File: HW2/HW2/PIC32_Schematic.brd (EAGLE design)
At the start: 50 x 50 mm, 22 parts

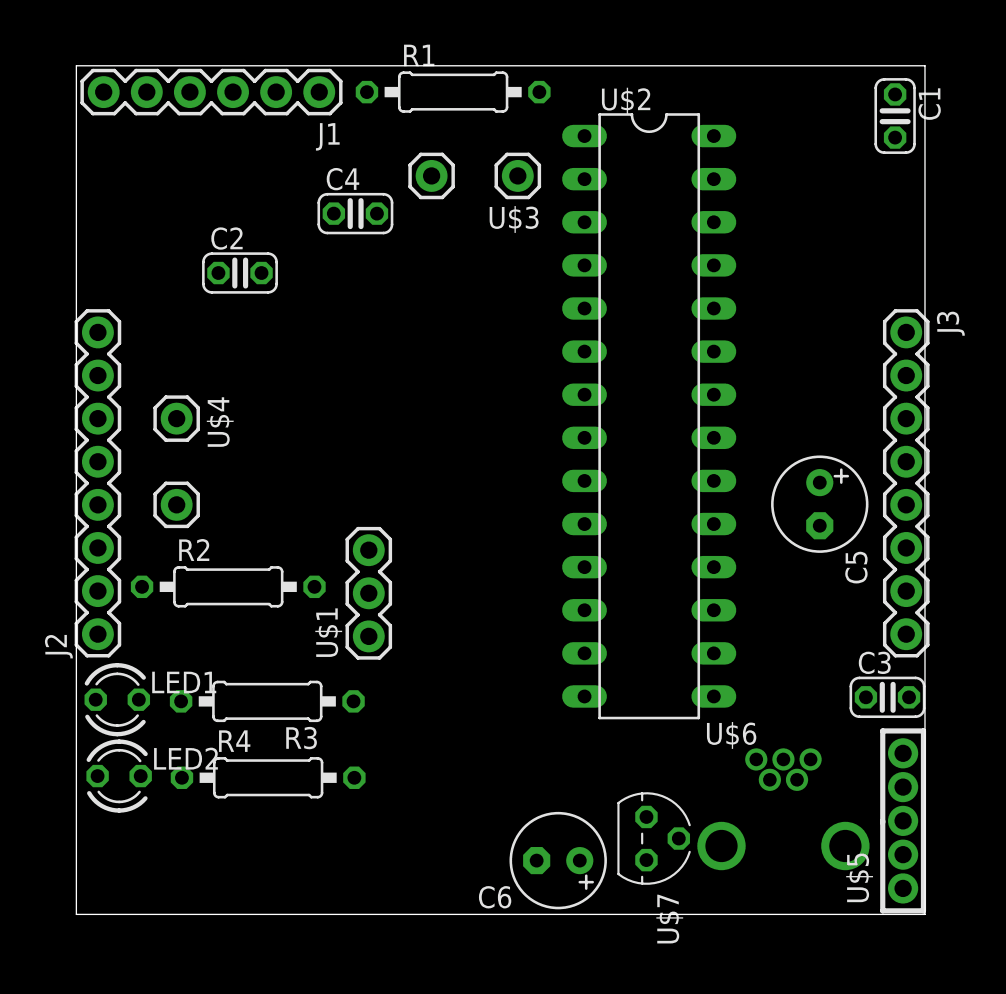
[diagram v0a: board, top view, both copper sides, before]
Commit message: All components placed relative to each other
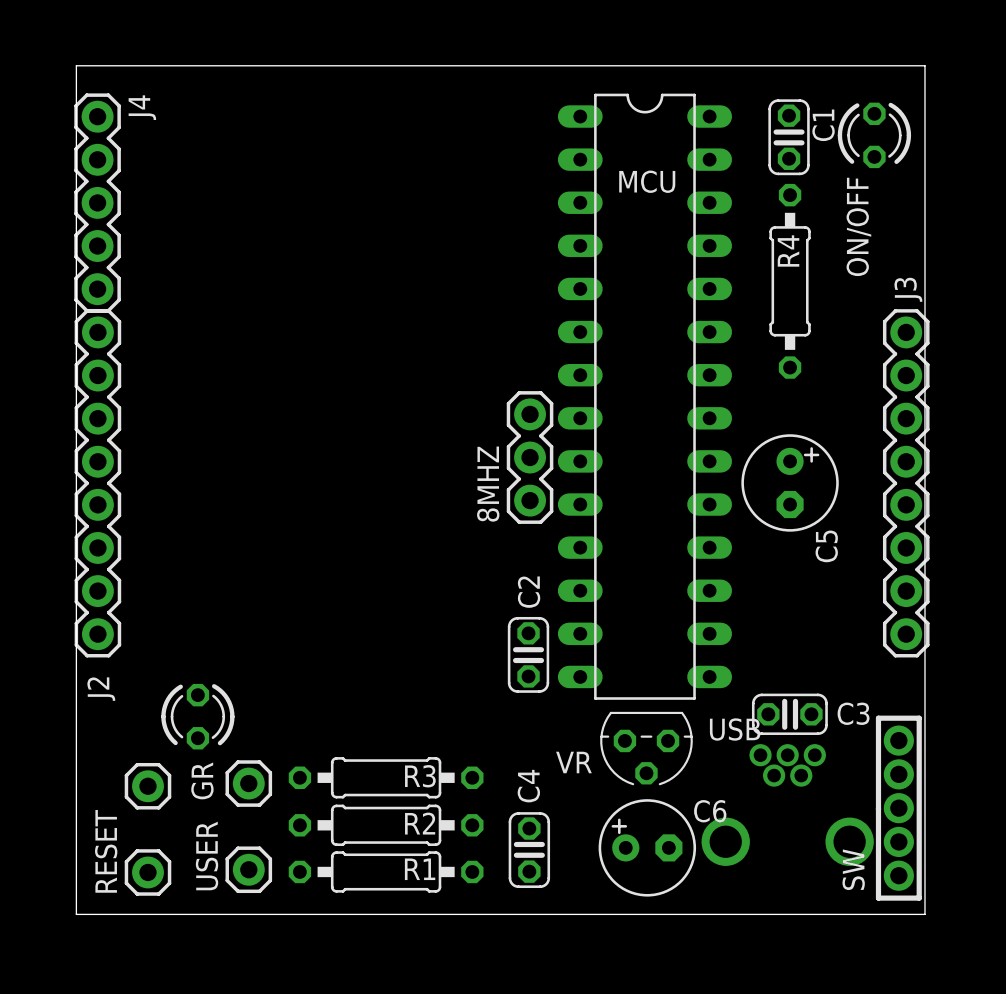
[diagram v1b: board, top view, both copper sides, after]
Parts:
- removed J1: (no value), ME433:1X06
- removed LED1: GREEN, ME433:LED3MM
- removed LED2: RED, ME433:LED3MM
- removed U$1: 8MHZ_XTAL, ME433:8MHZ_XTAL
- removed U$2: PIC32MX250F128B, ME433:DIL28-3
- removed U$3, U$4: PUSH-BUTTON, ME433:PUSH-BUTTON
- removed U$5: SLIDE_SWITCH, ME433:SLIDE_SWITCH
- removed U$6: USB-MB-H-5PIN, ME433:USB-MB-H
- removed U$7: MCP1702, ME433:TO92
- added 8MHZ: XTAL, ME433:8MHZ_XTAL
- added GR: RA4, ME433:LED3MM
- added J4: (no value), ME433:1X05
- added MCU: PIC32MX250F128B, ME433:DIL28-3
- added ON/OFF: (no value), ME433:LED3MM
- added RESET, USER: (no value), ME433:PUSH-BUTTON
- added SW: (no value), ME433:SLIDE_SWITCH
- added USB: USB-MB-H-5PIN, ME433:USB-MB-H
- added VR: MCP1702, ME433:TO92
- moved R1 46.1 mm to (18.2, 2.50)
- moved R4 42.4 mm to (42.0, 37.3), turned to 270 degrees
- moved C4 38.9 mm to (26.7, 3.79), turned to 90 degrees
- moved C2 28.2 mm to (26.6, 15.3), turned to 270 degrees
- moved R2 16.8 mm to (18.2, 5.25), turned to 180 degrees
- moved R3 8.32 mm to (18.2, 8.05)
- moved C1 6.37 mm to (42.0, 45.8)
- moved C3 5.84 mm to (42.0, 11.8)
- moved C6 5.30 mm to (33.6, 3.92), turned to 0 degrees
- moved C5 2.15 mm to (42.0, 25.4)
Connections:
- net +3V3: now also J4.2, MCU.13, MCU.23, MCU.28, ON/OFF.A, VR.3; no longer J1.2, LED2.A, U$2.13, U$2.23, U$2.28, U$7.3
- net +5V: now also MCU.15, SW.4, VR.2; no longer U$2.15, U$5.4, U$7.2
- net A0: now also MCU.2; no longer U$2.2
- net A1: now also MCU.3; no longer U$2.3
- net A2: now also 8MHZ.3, MCU.9; no longer U$1.3, U$2.9
- net A3: now also 8MHZ.1, MCU.10; no longer U$1.1, U$2.10
- net A4: now also GR.A, MCU.12; no longer LED1.A, U$2.12
- net B0: now also J4.4, MCU.4; no longer J1.4, U$2.4
- net B1: now also J4.5, MCU.5; no longer J1.5, U$2.5
- net B13: now also MCU.24; no longer U$2.24
- net B14: now also MCU.25; no longer U$2.25
- net B15: now also MCU.26; no longer U$2.26
- net B2: now also MCU.6; no longer U$2.6
- net B3: now also MCU.7; no longer U$2.7
- net B4: now also MCU.11, USER.3; no longer U$2.11, U$4.3
- net B7: now also MCU.16; no longer U$2.16
- net B8: now also MCU.17; no longer U$2.17
- net B9: now also MCU.18; no longer U$2.18
- net D+: now also MCU.21, USB.D+; no longer U$2.21, U$6.D+
- net D-: now also MCU.22, USB.D-; no longer U$2.22, U$6.D-
- net GND: now also 8MHZ.2, J4.3, MCU.19, MCU.27, MCU.8, RESET.1, USB.GND, USER.1, VR.1; no longer J1.3, U$1.2, U$2.19, U$2.27, U$2.8, U$3.1, U$4.1, U$6.GND, U$7.1
- net GREENLED: now also GR.K; no longer LED1.K
- net ID: now also MCU.14, USB.ID; no longer U$2.14, U$6.ID
- net MCLR: now also J4.1, MCU.1, RESET.3; no longer J1.1, U$2.1, U$3.3
- net N$3: now also ON/OFF.K; no longer LED2.K
- net N$9: now also MCU.20; no longer U$2.20
- net VBUS: now also SW.3, USB.VBUS; no longer U$5.3, U$6.VBUS

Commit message: Ground and +3.3V planes added (bottom and top)
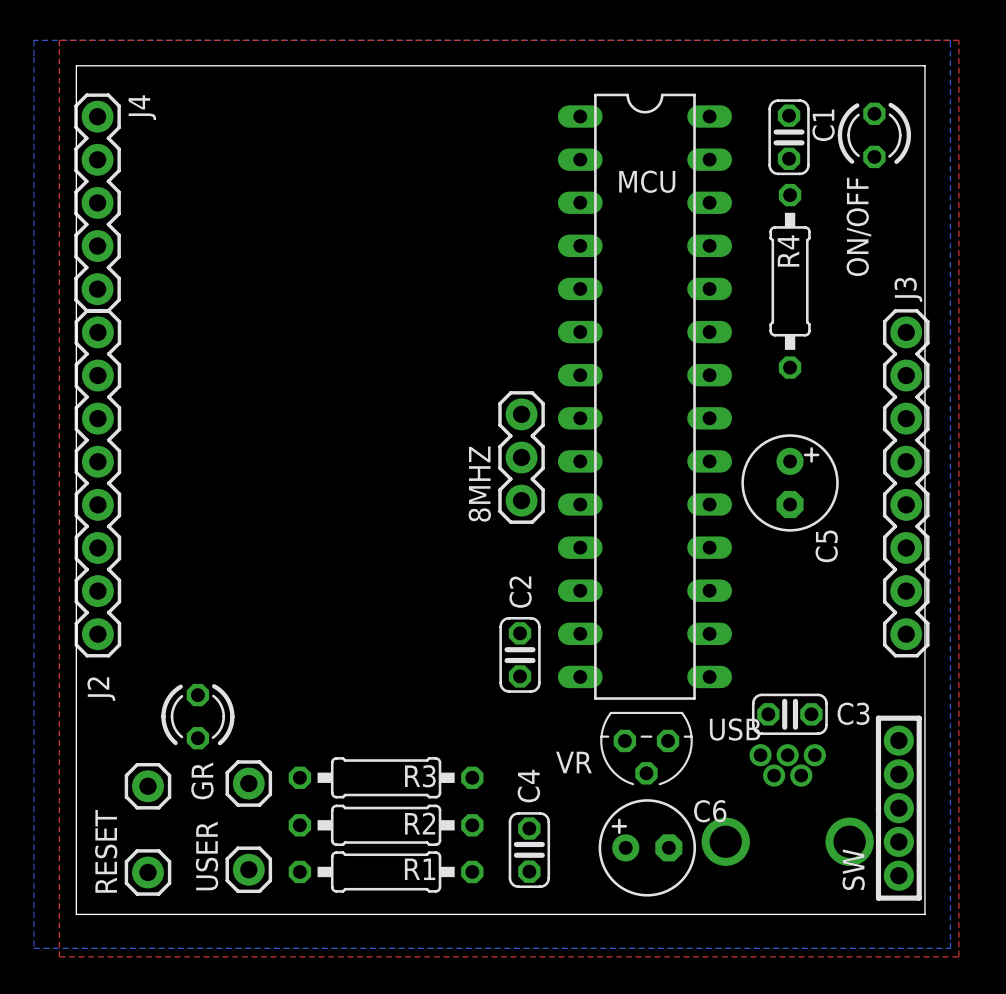
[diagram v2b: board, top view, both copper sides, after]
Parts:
- moved 8MHZ 0.50 mm to (26.2, 26.9)
- moved C2 0.50 mm to (26.1, 15.3)
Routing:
- added copper zone on layer 1, net +3V3
- added copper zone on layer 16, net GND
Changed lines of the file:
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@@
 <layers>
 <layer number="1" name="Top" color="4" fill="1" visible="yes" active="yes"/>
-<layer number="16" name="Bottom" color="1" fill="1" visible="yes" active="yes"/>
+<layer number="16" name="GND" color="1" fill="1" visible="yes" active="yes"/>
 <layer number="17" name="Pads" color="2" fill="1" visible="yes" active="yes"/>
 <layer number="18" name="Vias" color="2" fill="1" visible="yes" active="yes"/>
@@
 <layer number="27" name="tValues" color="7" fill="1" visible="yes" active="yes"/>
 <layer number="28" name="bValues" color="7" fill="1" visible="yes" active="yes"/>
-<layer number="29" name="tStop" color="7" fill="3" visible="no" active="yes"/>
-<layer number="30" name="bStop" color="7" fill="6" visible="no" active="yes"/>
-<layer number="31" name="tCream" color="7" fill="4" visible="no" active="yes"/>
-<layer number="32" name="bCream" color="7" fill="5" visible="no" active="yes"/>
-<layer number="33" name="tFinish" color="6" fill="3" visible="no" active="yes"/>
-<layer number="34" name="bFinish" color="6" fill="6" visible="no" active="yes"/>
-<layer number="35" name="tGlue" color="7" fill="4" visible="no" active="yes"/>
-<layer number="36" name="bGlue" color="7" fill="5" visible="no" active="yes"/>
-<layer number="37" name="tTest" color="7" fill="1" visible="no" active="yes"/>
-<layer number="38" name="bTest" color="7" fill="1" visible="no" active="yes"/>
+<layer number="29" name="tStop" color="7" fill="3" visible="yes" active="yes"/>
+<layer number="30" name="bStop" color="7" fill="6" visible="yes" active="yes"/>
+<layer number="31" name="tCream" color="7" fill="4" visible="yes" active="yes"/>
+<layer number="32" name="bCream" color="7" fill="5" visible="yes" active="yes"/>
+<layer number="33" name="tFinish" color="6" fill="3" visible="yes" active="yes"/>
+<layer number="34" name="bFinish" color="6" fill="6" visible="yes" active="yes"/>
+<layer number="35" name="tGlue" color="7" fill="4" visible="yes" active="yes"/>
+<layer number="36" name="bGlue" color="7" fill="5" visible="yes" active="yes"/>
+<layer number="37" name="tTest" color="7" fill="1" visible="yes" active="yes"/>
+<layer number="38" name="bTest" color="7" fill="1" visible="yes" active="yes"/>
 <layer number="39" name="tKeepout" color="4" fill="11" visible="yes" active="yes"/>
 <layer number="40" name="bKeepout" color="1" fill="11" visible="yes" active="yes"/>
@@
 <layer number="42" name="bRestrict" color="1" fill="10" visible="yes" active="yes"/>
 <layer number="43" name="vRestrict" color="2" fill="10" visible="yes" active="yes"/>
-<layer number="44" name="Drills" color="7" fill="1" visible="no" active="yes"/>
-<layer number="45" name="Holes" color="7" fill="1" visible="no" active="yes"/>
-<layer number="46" name="Milling" color="3" fill="1" visible="no" active="yes"/>
-<layer number="47" name="Measures" color="7" fill="1" visible="no" active="yes"/>
+<layer number="44" name="Drills" color="7" fill="1" visible="yes" active="yes"/>
+<layer number="45" name="Holes" color="7" fill="1" visible="yes" active="yes"/>
+<layer number="46" name="Milling" color="3" fill="1" visible="yes" active="yes"/>
+<layer number="47" name="Measures" color="7" fill="1" visible="yes" active="yes"/>
 <layer number="48" name="Document" color="7" fill="1" visible="yes" active="yes"/>
 <layer number="49" name="Reference" color="7" fill="1" visible="yes" active="yes"/>
@@
 <elements>
 <element name="C1" library="ME433" package="C025-024X044" value="0.1uF" x="41.99" y="45.79" rot="R270"/>
-<element name="C2" library="ME433" package="C025-024X044" value="0.1uF" x="26.64" y="15.29" smashed="yes" rot="R270">
-<attribute name="NAME" x="26.037" y="20.068" size="1.27" layer="25" ratio="10" rot="R270"/>
-<attribute name="VALUE" x="23.973" y="17.068" size="1.27" layer="27" ratio="10" rot="R270"/>
+<element name="C2" library="ME433" package="C025-024X044" value="0.1uF" x="26.14" y="15.29" smashed="yes" rot="R270">
+<attribute name="NAME" x="25.537" y="20.068" size="1.27" layer="25" ratio="10" rot="R270"/>
+<attribute name="VALUE" x="23.473" y="17.068" size="1.27" layer="27" ratio="10" rot="R270"/>
 </element>
 <element name="C3" library="ME433" package="C025-024X044" value="0.1uF" x="42.04" y="11.79" smashed="yes">
@@
 <attribute name="VALUE" x="41.665" y="37.3106" size="1.27" layer="27" ratio="10" rot="R270"/>
 </element>
-<element name="8MHZ" library="ME433" package="8MHZ_XTAL" value="XTAL" x="26.73" y="26.92" smashed="yes" rot="R90">
-<attribute name="NAME" x="24.9012" y="23.0338" size="1.27" layer="25" ratio="10" rot="R90"/>
-<attribute name="VALUE" x="24.905" y="28.11" size="1.27" layer="27" rot="R90"/>
+<element name="8MHZ" library="ME433" package="8MHZ_XTAL" value="XTAL" x="26.23" y="26.92" smashed="yes" rot="R90">
+<attribute name="NAME" x="24.4012" y="23.0338" size="1.27" layer="25" ratio="10" rot="R90"/>
+<attribute name="VALUE" x="24.405" y="28.11" size="1.27" layer="27" rot="R90"/>
 </element>
 <element name="MCU" library="ME433" package="DIL28-3" value="PIC32MX250F128B" x="33.5" y="30.5" smashed="yes" rot="R270">
@@
 <contactref element="VR" pad="2"/>
 <contactref element="C3" pad="1"/>
-<wire x1="40.77" y1="11.79" x2="48.895" y2="19.05" width="0" layer="19" extent="1-1"/>
+<wire x1="48.46" y1="8.25" x2="48.895" y2="19.05" width="0" layer="19" extent="1-1"/>
+<wire x1="40.77" y1="11.79" x2="48.46" y2="8.25" width="0" layer="19" extent="1-1"/>
 <wire x1="37.31" y1="13.99" x2="40.77" y2="11.79" width="0" layer="19" extent="1-1"/>
 <wire x1="33.59" y1="8.315" x2="37.31" y2="13.99" width="0" layer="19" extent="1-1"/>
-<wire x1="48.46" y1="8.25" x2="40.77" y2="11.79" width="0" layer="19" extent="1-1"/>
 </signal>
 <signal name="A3">
 <contactref element="MCU" pad="10"/>
 <contactref element="8MHZ" pad="1"/>
-<wire x1="26.73" y1="24.38" x2="29.69" y2="24.15" width="0" layer="19" extent="1-1"/>
+<wire x1="26.23" y1="24.38" x2="29.69" y2="24.15" width="0" layer="19" extent="1-1"/>
 </signal>
 <signal name="A1">
@@
 <contactref element="C4" pad="1"/>
 <contactref element="J4" pad="2"/>
-<wire x1="41.99" y1="47.06" x2="47.02" y2="47.17" width="0" layer="19" extent="1-1"/>
-<wire x1="37.31" y1="47.01" x2="41.99" y2="47.06" width="0" layer="19" extent="1-1"/>
-<wire x1="37.31" y1="34.31" x2="37.31" y2="47.01" width="0" layer="19" extent="1-1"/>
-<wire x1="29.69" y1="16.53" x2="37.31" y2="34.31" width="0" layer="19" extent="1-1"/>
-<wire x1="26.64" y1="16.56" x2="29.69" y2="16.53" width="0" layer="19" extent="1-1"/>
-<wire x1="32.32" y1="10.22" x2="29.69" y2="16.53" width="0" layer="19" extent="1-1"/>
-<wire x1="32.37" y1="3.92" x2="32.32" y2="10.22" width="0" layer="19" extent="1-1"/>
-<wire x1="26.69" y1="2.52" x2="32.37" y2="3.92" width="0" layer="19" extent="1-1"/>
-<wire x1="23.33" y1="2.5" x2="26.69" y2="2.52" width="0" layer="19" extent="1-1"/>
-<wire x1="23.33" y1="5.25" x2="23.33" y2="2.5" width="0" layer="19" extent="1-1"/>
-<wire x1="1.27" y1="19.05" x2="26.64" y2="16.56" width="0" layer="19" extent="1-1"/>
-<wire x1="1.25" y1="44.46" x2="1.27" y2="19.05" width="0" layer="19" extent="1-1"/>
+<polygon width="0.4064" layer="1">
+<vertex x="-1" y="51"/>
+<vertex x="-1" y="-2.5"/>
+<vertex x="52" y="-2.5"/>
+<vertex x="52" y="51.5"/>
+<vertex x="-1" y="51.5"/>
+</polygon>
 </signal>
 <signal name="GND" airwireshidden="yes">
@@
 <contactref element="C3" pad="2"/>
 <contactref element="J4" pad="3"/>
-<wire x1="37.31" y1="44.47" x2="41.99" y2="44.52" width="0" layer="19" extent="1-1"/>
-<wire x1="42.05" y1="32.22" x2="41.99" y2="44.52" width="0" layer="19" extent="1-1"/>
-<wire x1="42.05" y1="24.15" x2="42.05" y2="32.22" width="0" layer="19" extent="1-1"/>
-<wire x1="37.31" y1="24.15" x2="42.05" y2="24.15" width="0" layer="19" extent="1-1"/>
-<wire x1="43.31" y1="11.79" x2="42.05" y2="24.15" width="0" layer="19" extent="1-1"/>
-<wire x1="48.895" y1="16.51" x2="43.31" y2="11.79" width="0" layer="19" extent="1-1"/>
-<wire x1="43.51" y1="9.38" x2="43.31" y2="11.79" width="0" layer="19" extent="1-1"/>
-<wire x1="34.86" y1="10.22" x2="43.51" y2="9.38" width="0" layer="19" extent="1-1"/>
-<wire x1="34.91" y1="3.92" x2="34.86" y2="10.22" width="0" layer="19" extent="1-1"/>
-<wire x1="26.69" y1="5.06" x2="34.91" y2="3.92" width="0" layer="19" extent="1-1"/>
-<wire x1="23.33" y1="8.05" x2="26.69" y2="5.06" width="0" layer="19" extent="1-1"/>
-<wire x1="26.64" y1="14.02" x2="23.33" y2="8.05" width="0" layer="19" extent="1-1"/>
-<wire x1="29.69" y1="29.23" x2="37.31" y2="24.15" width="0" layer="19" extent="1-1"/>
-<wire x1="26.73" y1="26.92" x2="29.69" y2="29.23" width="0" layer="19" extent="1-1"/>
-<wire x1="10.16" y1="2.63" x2="23.33" y2="8.05" width="0" layer="19" extent="1-1"/>
-<wire x1="4.22" y1="2.47" x2="10.16" y2="2.63" width="0" layer="19" extent="1-1"/>
-<wire x1="1.27" y1="16.51" x2="4.22" y2="2.47" width="0" layer="19" extent="1-1"/>
-<wire x1="1.25" y1="41.92" x2="1.27" y2="16.51" width="0" layer="19" extent="1-1"/>
+<polygon width="0.4064" layer="16">
+<vertex x="-2.5" y="50.5"/>
+<vertex x="-2.5" y="-2"/>
+<vertex x="51.5" y="-2"/>
+<vertex x="51.5" y="-1.5"/>
+<vertex x="51.5" y="51.5"/>
+<vertex x="-2.5" y="51.5"/>
+</polygon>
 </signal>
 <signal name="A0">
@@
 <contactref element="8MHZ" pad="3"/>
 <contactref element="MCU" pad="9"/>
-<wire x1="29.69" y1="26.69" x2="26.73" y2="29.46" width="0" layer="19" extent="1-1"/>
+<wire x1="29.69" y1="26.69" x2="26.23" y2="29.46" width="0" layer="19" extent="1-1"/>
 </signal>
 </signals>

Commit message: Most connection wired...
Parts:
- moved C5 2.50 mm to (42.0, 27.9), turned to 90 degrees
- moved C3 2.26 mm to (41.8, 14.0)
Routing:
- net MCLR: track 0.00 -> 111.7 mm, vias 0 -> 3
- net B4: track 0.00 -> 46.3 mm
- net A4: track 0.00 -> 35.1 mm
- net A1: track 0.00 -> 32.6 mm
- net A0: track 0.00 -> 32.6 mm
- net B3: track 0.00 -> 30.5 mm
- net B2: track 0.00 -> 30.5 mm
- net B1: track 0.00 -> 28.4 mm
- net B0: track 0.00 -> 28.4 mm
- net +5V: track 0.00 -> 23.1 mm
- net ID: track 0.00 -> 19.9 mm
- net B15: track 0.00 -> 14.7 mm
- net B14: track 0.00 -> 14.7 mm
- net B13: track 0.00 -> 14.7 mm
- net VBUS: track 0.00 -> 13.8 mm
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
